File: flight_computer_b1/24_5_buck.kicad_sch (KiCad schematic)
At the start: 9 parts, among them U5 LMR51430XDDCR

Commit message: flight computer: added mux and voltage sense channels
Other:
- company: (none) -> Purdue Space Program Liquids
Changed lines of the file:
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@@
 	(generator_version "9.0")
 	(paper "A4")
+	(title_block
+		(date "2025-11-05")
+		(rev "1")
+		(company "Purdue Space Program Liquids")
+	)
 	(text "Feedback resistors get us 5.1V"
 		(exclude_from_sim no)

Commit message: flight computer: added pyro circuit and digikey part numbers
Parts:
- L1: DIGIKEY PART N (none) -> 445-174172-1-ND
- U5: DIGIKEY PART N (none) -> 296-LMR51430XDDCRCT-ND
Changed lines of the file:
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@@
+			)
+		)
+		(property "DIGIKEY PART N" ""
+			(at 167.64 110.49 0)
+			(effects
+				(font
+					(size 1.27 1.27)
+				)
+				(hide yes)
 			)
 		)
@@
 			)
 		)
+		(property "DIGIKEY PART N" ""
+			(at 167.64 88.9 0)
+			(effects
+				(font
+					(size 1.27 1.27)
+				)
+				(hide yes)
+			)
+		)
 		(pin "2"
 		)
@@
 		)
 		(property "Description" "Unpolarized capacitor, small symbol"
+			(at 181.61 87.63 0)
+			(effects
+				(font
+					(size 1.27 1.27)
+				)
+				(hide yes)
+			)
+		)
+		(property "DIGIKEY PART N" ""
 			(at 181.61 87.63 0)
 			(effects
@@
 			)
 		)
+		(property "DIGIKEY PART N" ""
+			(at 190.5 87.63 0)
+			(effects
+				(font
+					(size 1.27 1.27)
+				)
+				(hide yes)
+			)
+		)
 		(pin "2"
 		)
@@
 			)
 		)
+		(property "DIGIKEY PART N" "296-LMR51430XDDCRCT-ND"
+			(at 118.11 82.55 0)
+			(effects
+				(font
+					(size 1.27 1.27)
+				)
+				(hide yes)
+			)
+		)
 		(pin "5"
 		)
@@
 			)
 		)
+		(property "DIGIKEY PART N" "445-174172-1-ND"
+			(at 152.4 82.55 0)
+			(effects
+				(font
+					(size 1.27 1.27)
+				)
+				(hide yes)
+			)
+		)
 		(pin "1"
 		)
@@
 			)
 		)
+		(property "DIGIKEY PART N" ""
+			(at 167.64 97.79 0)
+			(effects
+				(font
+					(size 1.27 1.27)
+				)
+				(hide yes)
+			)
+		)
 		(pin "2"
 		)
@@
 			)
 		)
+		(property "DIGIKEY PART N" ""
+			(at 96.52 85.09 0)
+			(effects
+				(font
+					(size 1.27 1.27)
+				)
+				(hide yes)
+			)
+		)
 		(pin "2"
 		)
@@
 			(effects
 				(font
+					(size 1.27 1.27)
+				)
+				(hide yes)
+			)
+		)
+		(property "DIGIKEY PART N" ""
+			(at 134.62 80.01 90)
+			(effects
+				(font

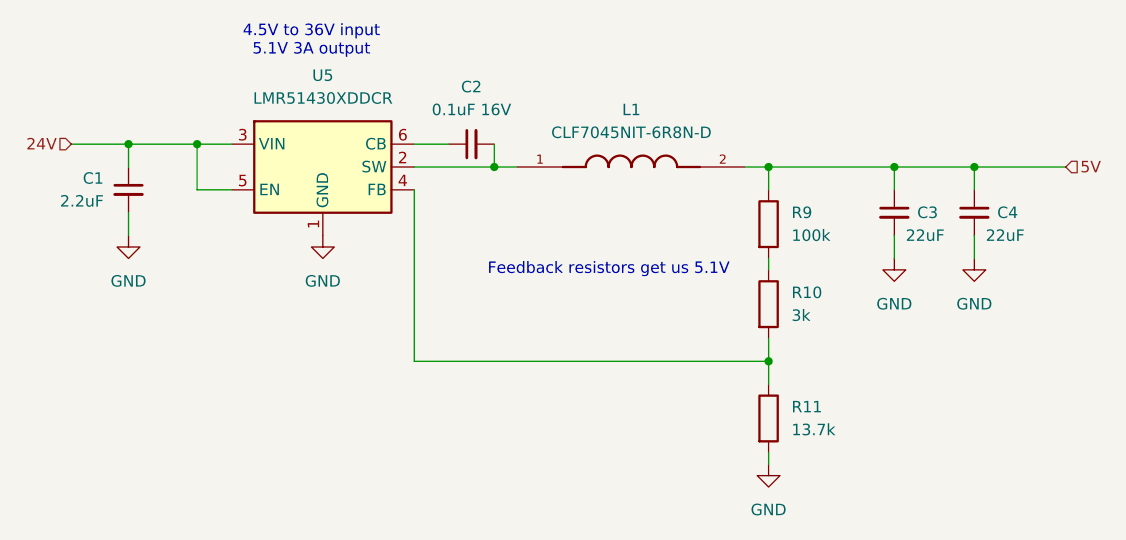
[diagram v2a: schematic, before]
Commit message: flight computer: routing updates
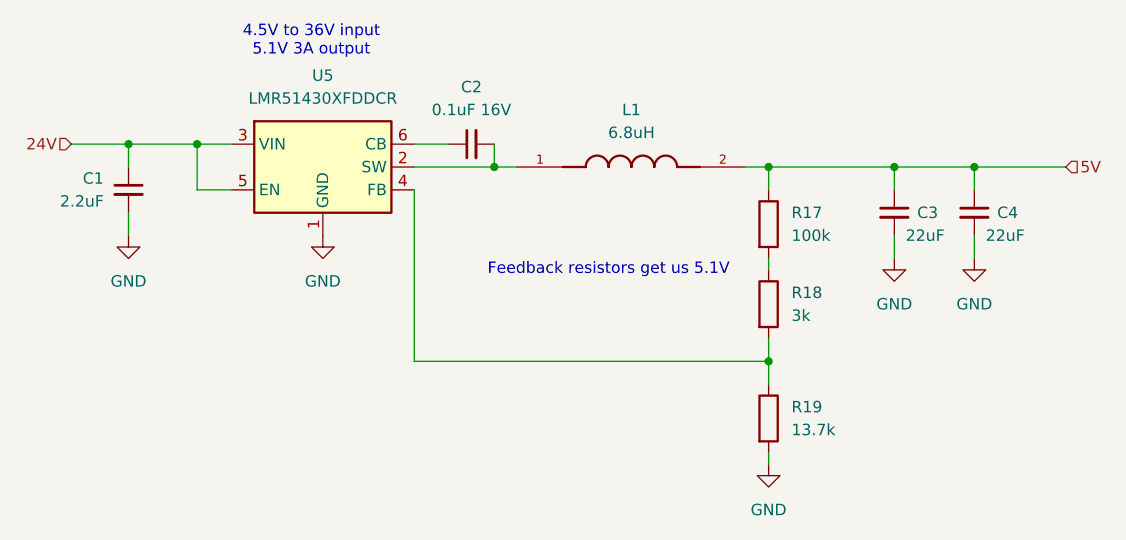
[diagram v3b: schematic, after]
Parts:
- L1: value CLF7045NIT-6R8N-D -> 6.8uH
- U5: value LMR51430XDDCR -> LMR51430XFDDCR; DIGIKEY PART N 296-LMR51430XDDCRCT-ND -> 296-LMR51430XFDDCRCT-ND
- renumbered R9 to R17, R10 to R18, R11 to R19
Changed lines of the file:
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@@
 		(dnp no)
 		(fields_autoplaced yes)
-		(property "Reference" "R11"
+		(property "Reference" "R19"
 			(at 170.18 109.2199 0)
 			(effects
@@
 			(project "flight_computer"
 				(path "/b71a7b79-cdb5-4e38-a72c-0daaa3474f05/45d05398-45d2-4c5e-8eda-8a352ba114a9"
-					(reference "R11")
+					(reference "R19")
 					(unit 1)
 				)
@@
 		(dnp no)
 		(fields_autoplaced yes)
-		(property "Reference" "#PWR034"
+		(property "Reference" "#PWR045"
 			(at 190.5 99.06 0)
 			(effects
@@
 			(project "flight_computer"
 				(path "/b71a7b79-cdb5-4e38-a72c-0daaa3474f05/45d05398-45d2-4c5e-8eda-8a352ba114a9"
-					(reference "#PWR034")
+					(reference "#PWR045")
 					(unit 1)
 				)
@@
 		(dnp no)
 		(fields_autoplaced yes)
-		(property "Reference" "R9"
+		(property "Reference" "R17"
 			(at 170.18 87.6299 0)
 			(effects
@@
 			(project "flight_computer"
 				(path "/b71a7b79-cdb5-4e38-a72c-0daaa3474f05/45d05398-45d2-4c5e-8eda-8a352ba114a9"
-					(reference "R9")
+					(reference "R17")
 					(unit 1)
 				)
@@
 		(dnp no)
 		(fields_autoplaced yes)
-		(property "Reference" "#PWR032"
+		(property "Reference" "#PWR043"
 			(at 167.64 121.92 0)
 			(effects
@@
 			(project "flight_computer"
 				(path "/b71a7b79-cdb5-4e38-a72c-0daaa3474f05/45d05398-45d2-4c5e-8eda-8a352ba114a9"
-					(reference "#PWR032")
+					(reference "#PWR043")
 					(unit 1)
 				)
@@
 		(dnp no)
 		(fields_autoplaced yes)
-		(property "Reference" "#PWR033"
+		(property "Reference" "#PWR044"
 			(at 181.61 99.06 0)
 			(effects
@@
 			(project "flight_computer"
 				(path "/b71a7b79-cdb5-4e38-a72c-0daaa3474f05/45d05398-45d2-4c5e-8eda-8a352ba114a9"
-					(reference "#PWR033")
+					(reference "#PWR044")
 					(unit 1)
 				)
@@
 		(dnp no)
 		(fields_autoplaced yes)
-		(property "Reference" "#PWR030"
+		(property "Reference" "#PWR041"
 			(at 96.52 96.52 0)
 			(effects
@@
 			(project "flight_computer"
 				(path "/b71a7b79-cdb5-4e38-a72c-0daaa3474f05/45d05398-45d2-4c5e-8eda-8a352ba114a9"
-					(reference "#PWR030")
+					(reference "#PWR041")
 					(unit 1)
 				)
@@
 			)
 		)
-		(property "Value" "LMR51430XDDCR"
+		(property "Value" "LMR51430XFDDCR"
 			(at 118.11 74.93 0)
 			(effects
@@
 			)
 		)
-		(property "DIGIKEY PART N" "296-LMR51430XDDCRCT-ND"
+		(property "DIGIKEY PART N" "296-LMR51430XFDDCRCT-ND"
 			(at 118.11 82.55 0)
 			(effects
@@
 			)
 		)
-		(property "Value" "CLF7045NIT-6R8N-D"
+		(property "Value" "6.8uH"
 			(at 152.4 78.74 0)
 			(effects
@@
 			)
 		)
-		(property "Description" ""
+		(property "Description" "CLF7045NIT-6R8N-D"
 			(at 152.4 82.55 0)
 			(effects
@@
 		(dnp no)
 		(fields_autoplaced yes)
-		(property "Reference" "R10"
+		(property "Reference" "R18"
 			(at 170.18 96.5199 0)
 			(effects
@@
 			(project "flight_computer"
 				(path "/b71a7b79-cdb5-4e38-a72c-0daaa3474f05/45d05398-45d2-4c5e-8eda-8a352ba114a9"
-					(reference "R10")
+					(reference "R18")
 					(unit 1)
 				)
@@
 		(dnp no)
 		(fields_autoplaced yes)
-		(property "Reference" "#PWR031"
+		(property "Reference" "#PWR042"
 			(at 118.11 96.52 0)
 			(effects
@@
 			(project "flight_computer"
 				(path "/b71a7b79-cdb5-4e38-a72c-0daaa3474f05/45d05398-45d2-4c5e-8eda-8a352ba114a9"
-					(reference "#PWR031")
-					(unit 1)
-				)
+					(reference "#PWR042")
+					(unit 1)
+				)
